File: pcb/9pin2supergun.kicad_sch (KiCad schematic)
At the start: 14 parts, among them U3 RP2040

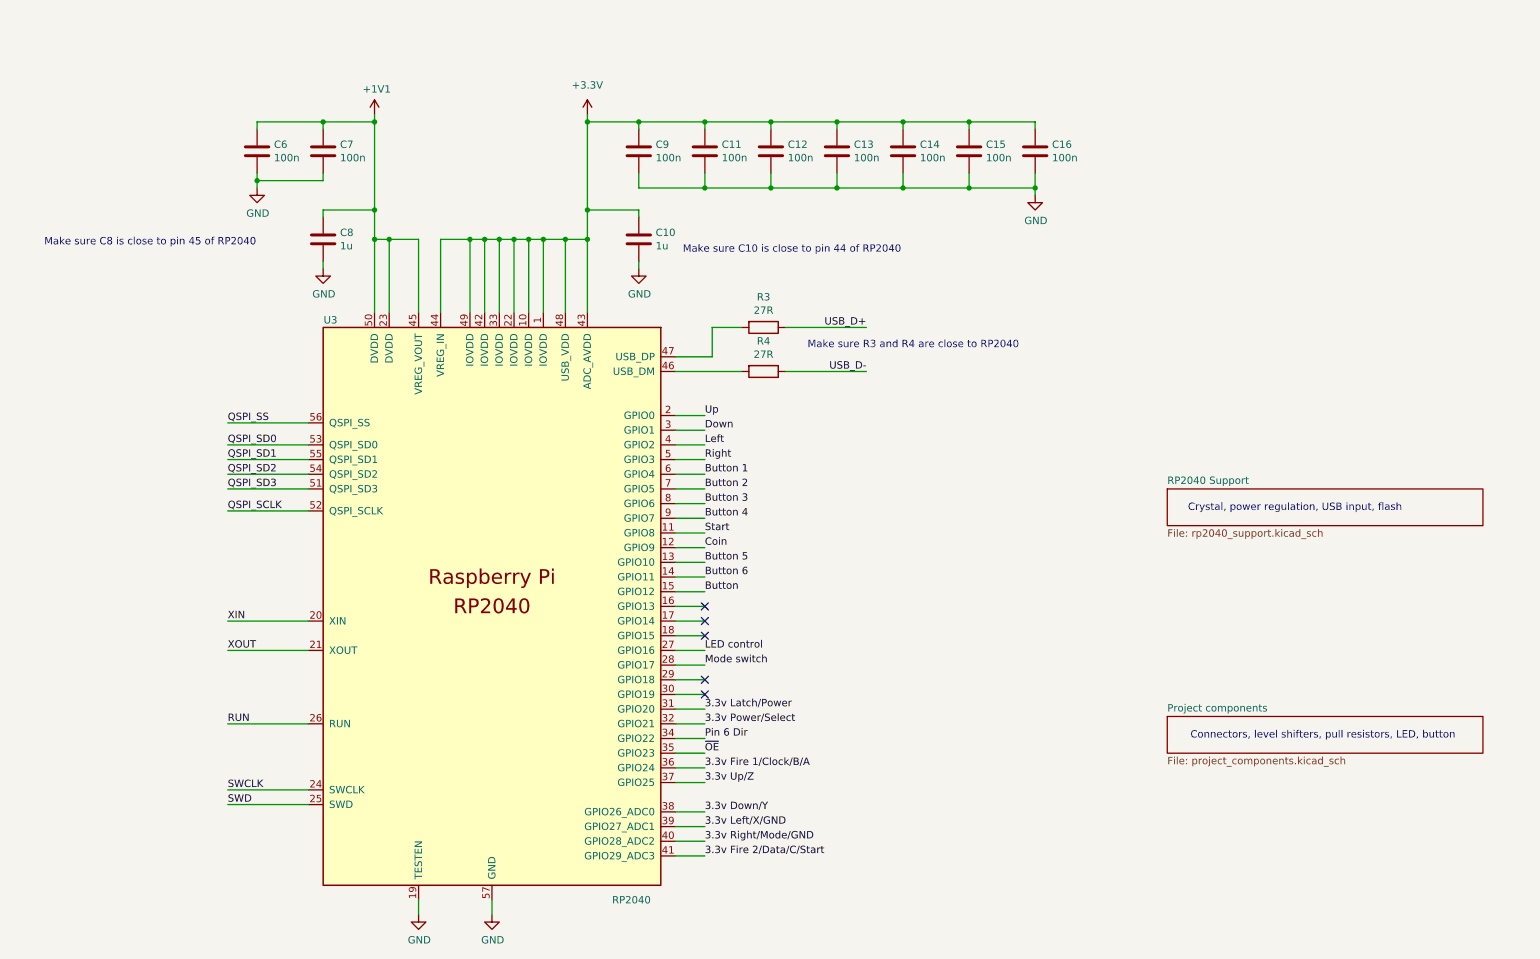
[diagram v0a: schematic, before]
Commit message: Update the schematic to properly use hierarchical sheets, update the PCB to match, tidy up some weirdnesses (button with a "U" refdes, both S and SW refdes, etc)
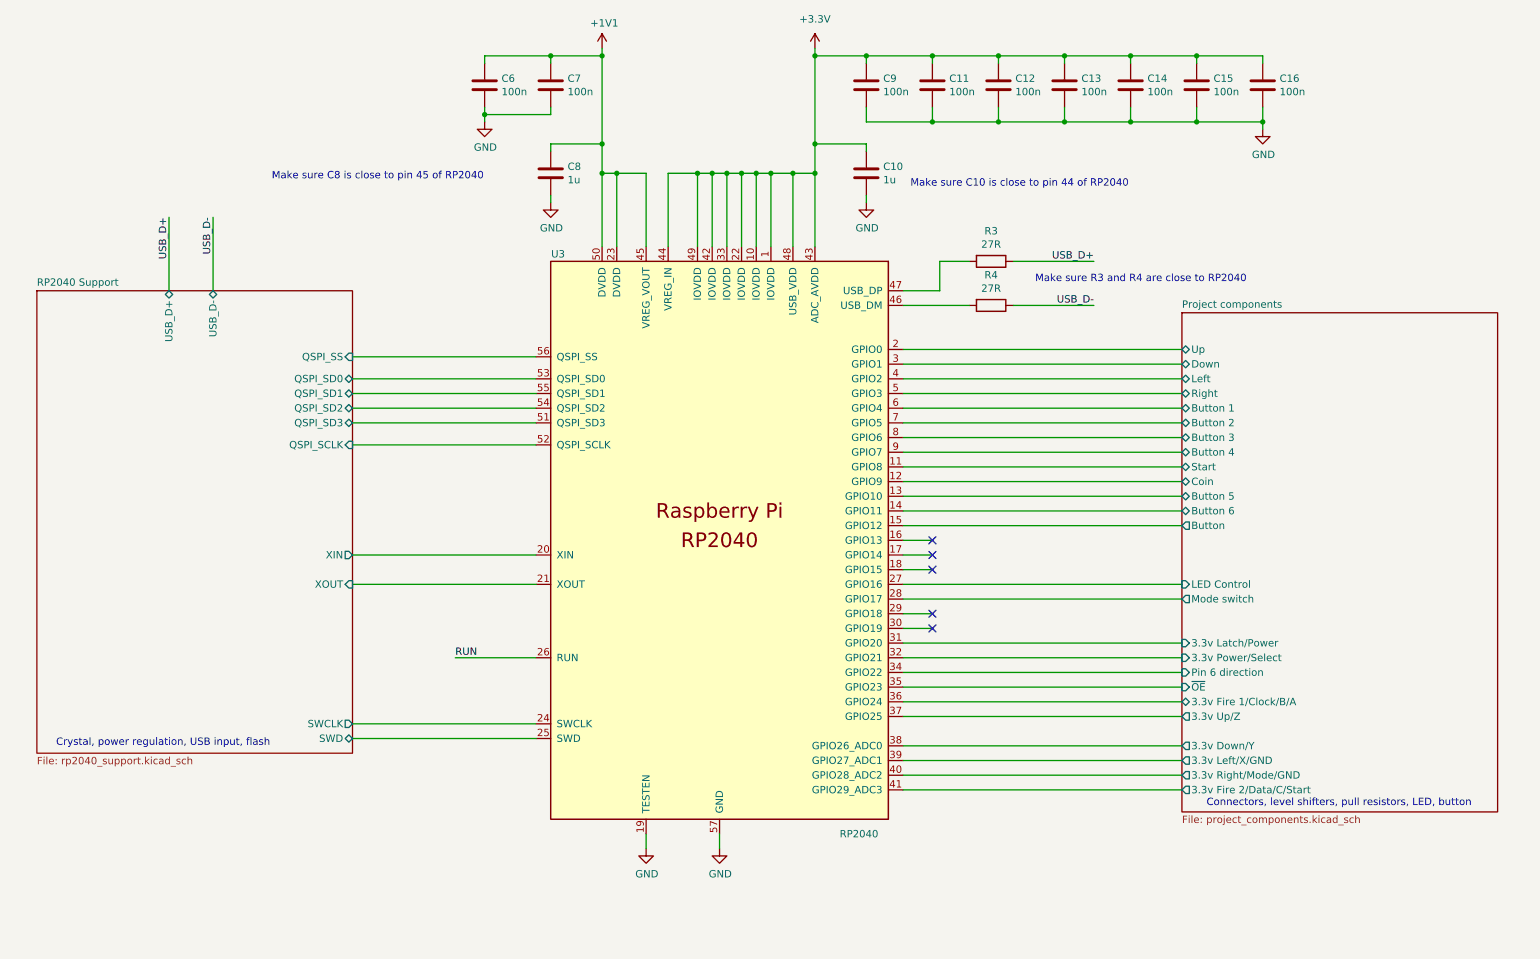
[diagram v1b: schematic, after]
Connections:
- net 3.3v Down/Y renamed Project components/3.3v Down/Y
- net 3.3v Fire 1/Clock/B/A renamed Project components/3.3v Fire 1/Clock/B/A
- net 3.3v Fire 2/Data/C/Start renamed Project components/3.3v Fire 2/Data/C/Start
- net 3.3v Latch/Power renamed Project components/3.3v Latch/Power
- net 3.3v Left/X/GND renamed Project components/3.3v Left/X/GND
- net 3.3v Power/Select renamed Project components/3.3v Power/Select
- net 3.3v Right/Mode/GND renamed Project components/3.3v Right/Mode/GND
- net 3.3v Up/Z renamed Project components/3.3v Up/Z
- net Button renamed Project components/Button
- net Button 1 renamed Project components/Button 1
- net Button 2 renamed Project components/Button 2
- net Button 3 renamed Project components/Button 3
- net Button 4 renamed Project components/Button 4
- net Button 5 renamed Project components/Button 5
- net Button 6 renamed Project components/Button 6
- net Coin renamed Project components/Coin
- net Down renamed Project components/Down
- net LED control renamed Project components/LED Control
- net Left renamed Project components/Left
- net Mode switch renamed Project components/Mode switch
- net Pin 6 Dir renamed Project components/Pin 6 direction
- net QSPI_SCLK renamed RP2040 Support/QSPI_SCLK
- net QSPI_SD0 renamed RP2040 Support/QSPI_SD0
- net QSPI_SD1 renamed RP2040 Support/QSPI_SD1
- net QSPI_SD2 renamed RP2040 Support/QSPI_SD2
- net QSPI_SD3 renamed RP2040 Support/QSPI_SD3
- net QSPI_SS renamed RP2040 Support/QSPI_SS
- net Right renamed Project components/Right
- net SWCLK renamed RP2040 Support/SWCLK
- net SWD renamed RP2040 Support/SWD
- net Start renamed Project components/Start
- net Up renamed Project components/Up
- net XIN renamed RP2040 Support/XIN
- net XOUT renamed RP2040 Support/XOUT
- net ~{OE} renamed Project components/~{OE}
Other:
- sheet Project components ports: added 3.3v Down/Y, 3.3v Fire 1/Clock/B/A, 3.3v Fire 2/Data/C/Start, 3.3v Latch/Power, 3.3v Left/X/GND, 3.3v Power/Select, 3.3v Right/Mode/GND, 3.3v Up/Z, Button, Button 1, Button 2, Button 3, Button 4, Button 5, Button 6, Coin, Down, LED Control, Left, Mode switch, Pin 6 direction, Right, Start, Up, ~{OE}; removed none
- sheet RP2040 Support ports: added QSPI_SCLK, QSPI_SD0, QSPI_SD1, QSPI_SD2, QSPI_SD3, QSPI_SS, SWCLK, SWD, USB_D+, USB_D-, XIN, XOUT; removed none
- moved on the sheet: C10, C11, C12, C13, C14, C15, C16, C6, C7, C8, C9, R3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
